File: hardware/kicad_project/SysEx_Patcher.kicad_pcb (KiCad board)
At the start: 2 copper layers, 135 x 118 mm, 83 parts, among them J1 MIDI_IN, J10 JACK6.35_pot_deporte, J2 MIDI_OUT, J3 DC_5V, J4 BAT_PWR, J5 OLED, J6 MEGA_AN, J7 MEGA_DIG, J8 MEGA_PWR, J9 MUX_SPARE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

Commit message: hardware: fully route the PCB (4 layers + GND plane)
Re-placed for routability (each RC filter beside its pot, 4067 inside the
board) and autorouted: 130/130 connections routed, DRC clean (no unconnected,
shorts, clearance or courtyard violations). 4-layer stackup with a GND plane.
Only cosmetic silkscreen-text overlaps remain.
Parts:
- removed J6: MEGA_AN, Connector_PinHeader_2.54mm:PinHeader_1x16_P2.54mm_Vertical
- removed J7: MEGA_DIG, Connector_PinHeader_2.54mm:PinHeader_1x16_P2.54mm_Vertical
- removed J9: MUX_SPARE, Connector_PinHeader_2.54mm:PinHeader_1x14_P2.54mm_Vertical
- added J6A: AN_row0, Connector_PinHeader_2.54mm:PinHeader_1x04_P2.54mm_Vertical, F.Cu at (186.0, 34.0)
- added J6B: AN_row1, Connector_PinHeader_2.54mm:PinHeader_1x04_P2.54mm_Vertical, F.Cu at (186.0, 64.0)
- added J6C: AN_row2, Connector_PinHeader_2.54mm:PinHeader_1x04_P2.54mm_Vertical, F.Cu at (186.0, 94.0)
- added J6D: AN_row3, Connector_PinHeader_2.54mm:PinHeader_1x04_P2.54mm_Vertical, F.Cu at (186.0, 124.0)
- added J7A: DIG_btnled, Connector_PinHeader_2.54mm:PinHeader_1x08_P2.54mm_Vertical, F.Cu at (34.0, 70.0)
- added J7B: DIG_midi, Connector_PinHeader_2.54mm:PinHeader_1x02_P2.54mm_Vertical, F.Cu at (130.0, 162.0)
- added J7C: DIG_i2c, Connector_PinHeader_2.54mm:PinHeader_1x02_P2.54mm_Vertical, F.Cu at (150.0, 162.0)
- added J7D: DIG_muxsel, Connector_PinHeader_2.54mm:PinHeader_1x04_P2.54mm_Vertical, F.Cu at (100.0, 150.0)
- J10: value JACK6.35_pot_deporte -> JACK6.35
- moved D2 247.0 mm to (188.0, 6.00)
- moved J4 236.3 mm to (195.0, 15.0)
- moved J5 206.5 mm to (150.0, 9.00)
- moved R2 172.2 mm to (132.0, 5.00)
- moved C1 170.8 mm to (96.0, 9.00)
- moved R3 163.2 mm to (132.0, 13.0)
- moved R25 157.3 mm to (159.0, 120.0), turned to 90 degrees
- moved C17 151.5 mm to (166.0, 120.0), turned to 90 degrees
- moved J8 147.7 mm to (160.0, 150.0)
- moved R21 139.5 mm to (159.0, 90.0), turned to 90 degrees
- moved C13 134.2 mm to (166.0, 90.0), turned to 90 degrees
- moved R20 132.4 mm to (125.0, 90.0), turned to 90 degrees
- moved R17 127.3 mm to (159.0, 60.0), turned to 90 degrees
- moved C12 127.1 mm to (132.0, 90.0), turned to 90 degrees
- moved C9 122.7 mm to (166.0, 60.0), turned to 90 degrees
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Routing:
- net +5V: track 0.00 -> 706.6 mm, vias 0 -> 1
- net VIN_RAW: track 0.00 -> 194.7 mm
- net D0_RX: track 0.00 -> 165.5 mm
- net D1_TX: track 0.00 -> 156.6 mm
- net D21_SCL: track 0.00 -> 152.3 mm
- net MUX_CH0: track 0.00 -> 150.0 mm, vias 0 -> 1
- net D20_SDA: track 0.00 -> 148.1 mm
- net A1: track 0.00 -> 142.1 mm
- net A2: track 0.00 -> 140.9 mm
- net A0: track 0.00 -> 137.7 mm
- net A3: track 0.00 -> 137.6 mm
- net A15: track 0.00 -> 123.6 mm
- net A4: track 0.00 -> 108.8 mm
- net A6: track 0.00 -> 107.8 mm
- net A5: track 0.00 -> 104.8 mm
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- added copper zone on B.Cu, net GND
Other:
- board size 135 x 118 mm -> 218 x 185 mm
- copper layers 2 -> 4

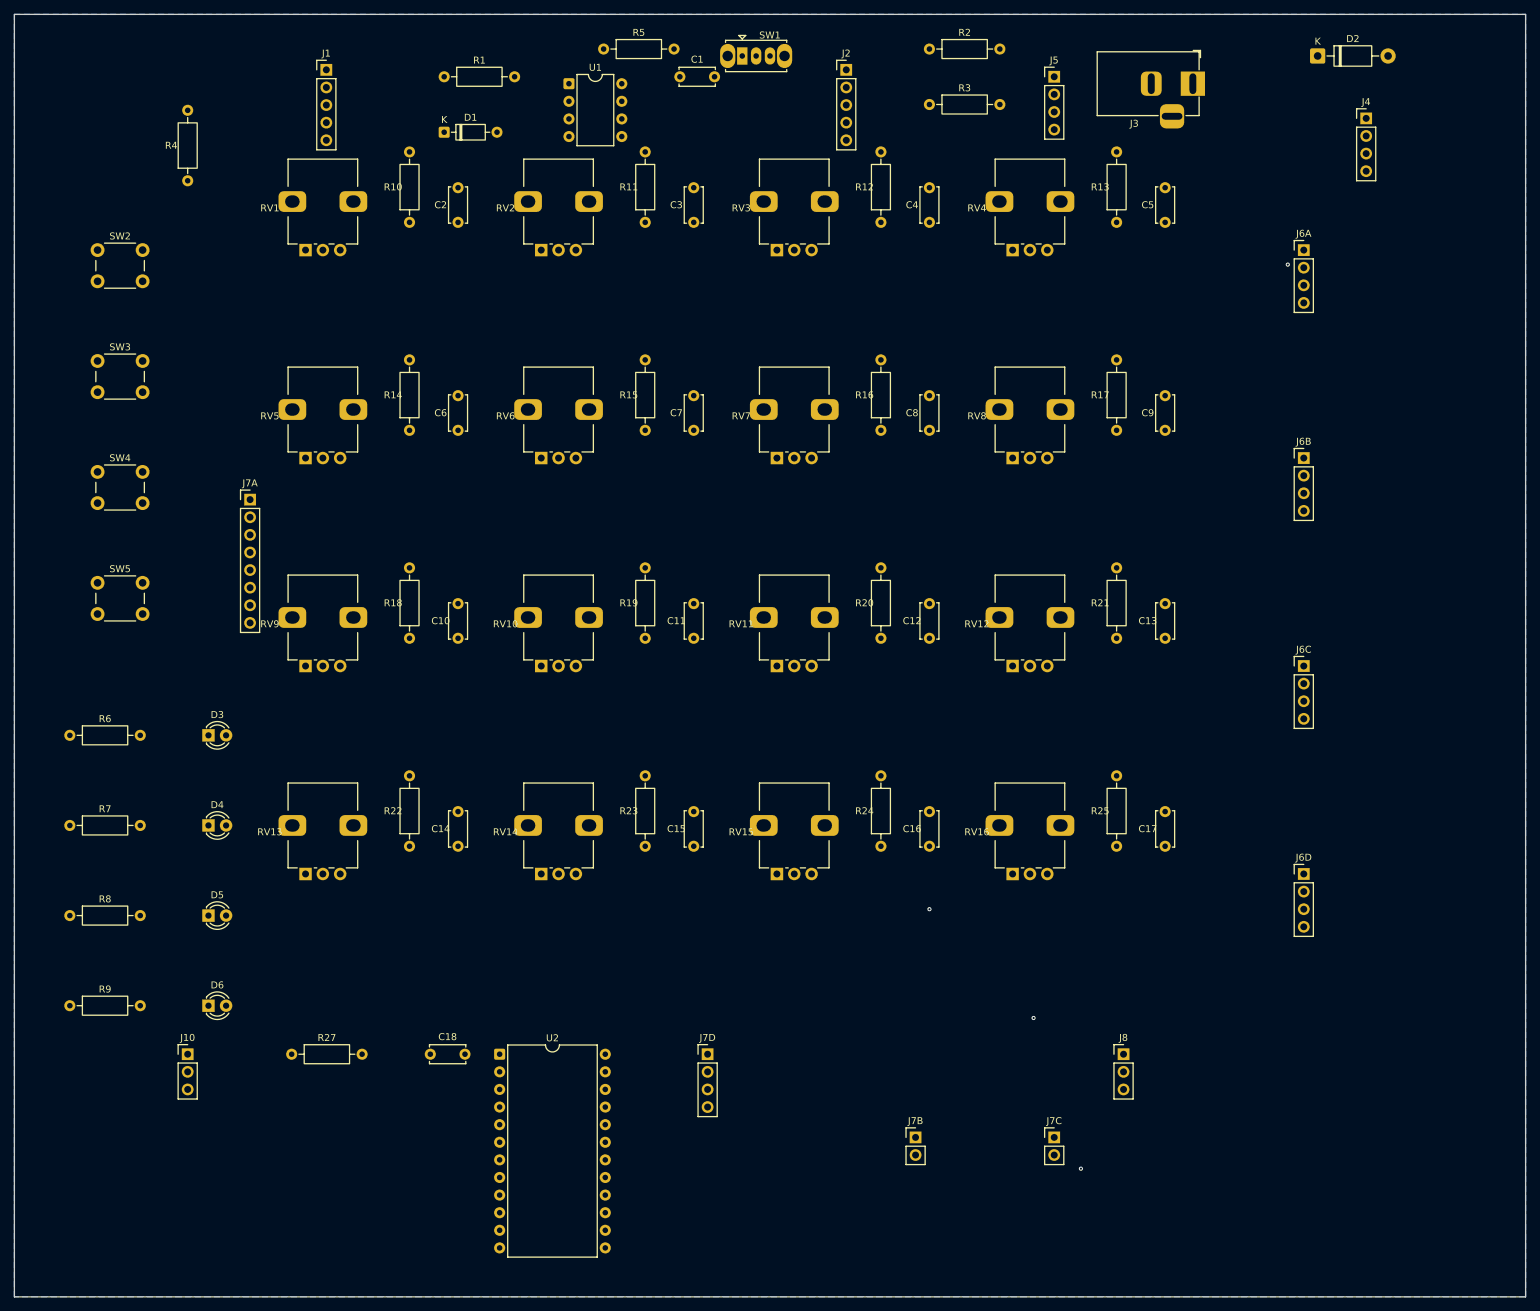
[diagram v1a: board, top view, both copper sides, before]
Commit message: hardware: compact board to 212x180mm, rounded corners, + fab Gerbers
Trimmed the board and added 5mm rounded corners (Edge.Cuts arcs). Re-routed
clean on the smaller outline (130/130 nets, DRC clean apart from cosmetic silk).
Added the fabrication package: 4-layer Gerbers + Excellon drill + job file
(hardware/fab/ and SysEx_Patcher_GERBERS.zip), ready for JLCPCB.
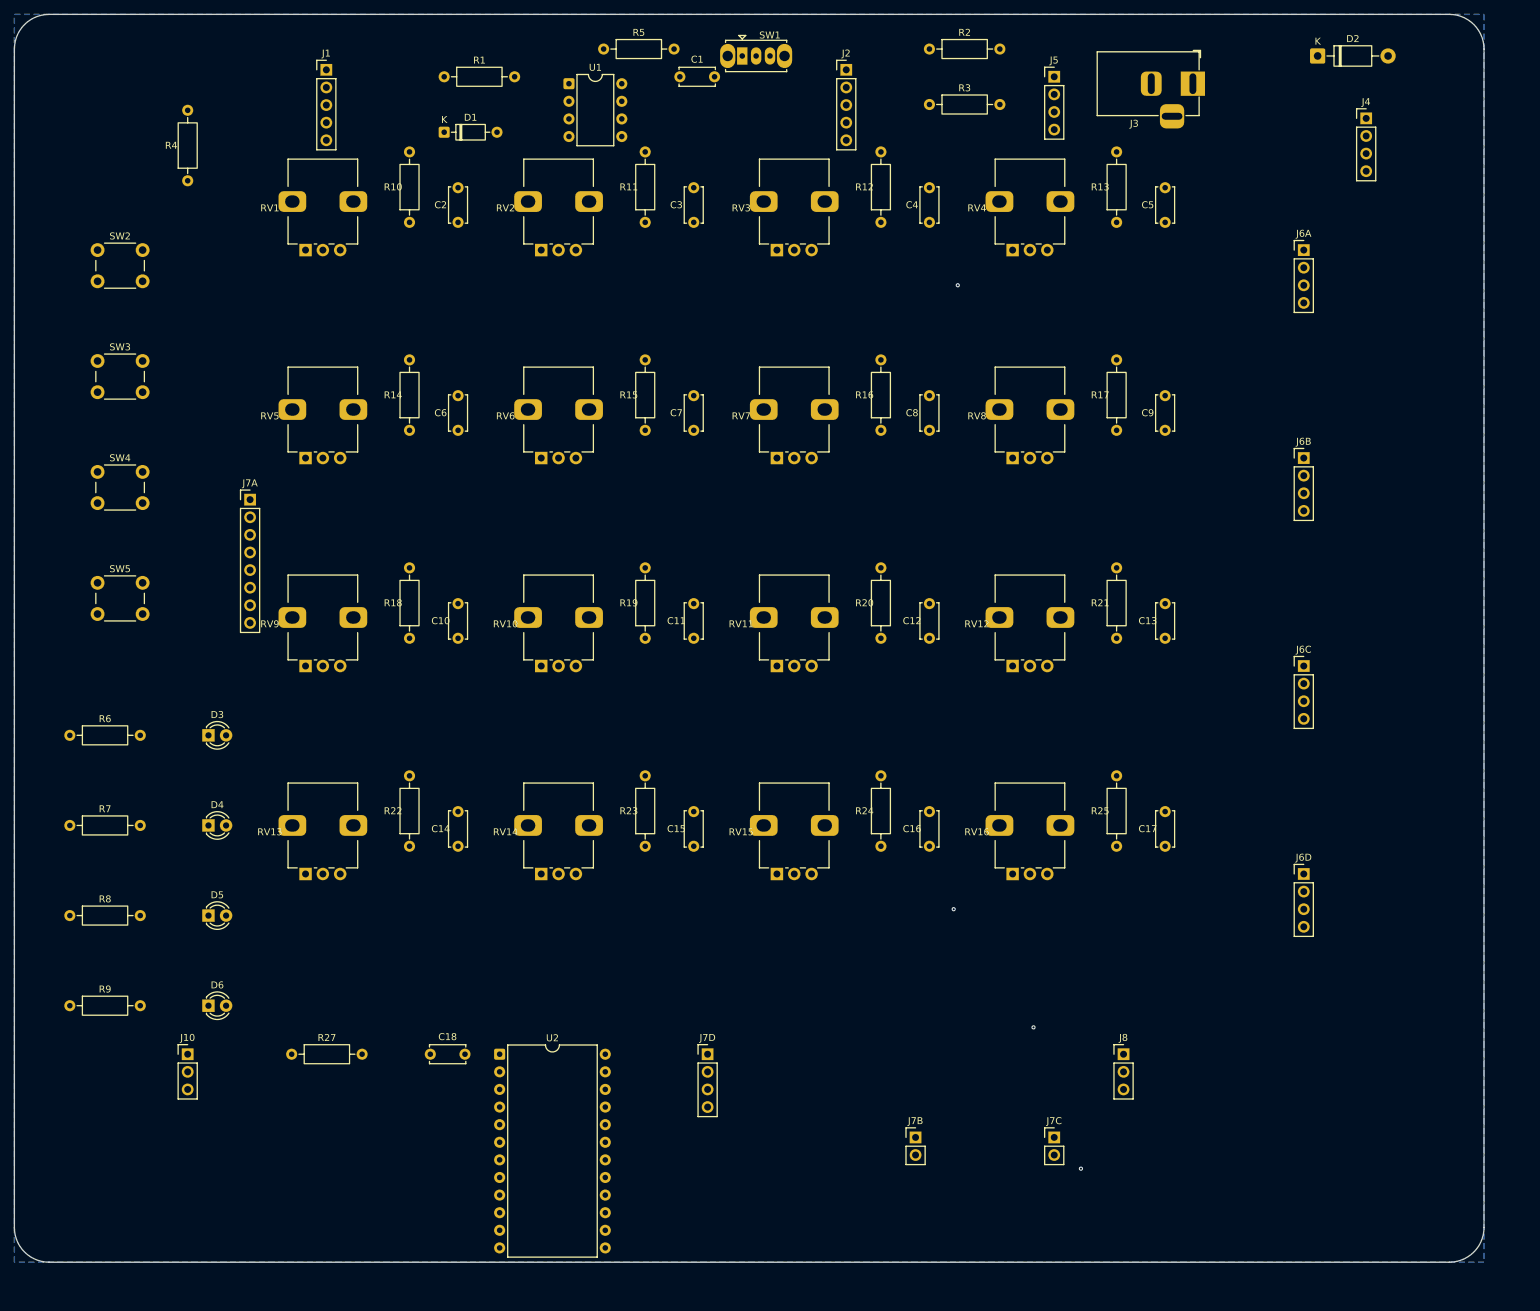
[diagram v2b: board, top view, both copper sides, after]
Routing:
- net A8: track 71.2 -> 73.7 mm
- net A11: track 76.1 -> 74.1 mm
- net A1: track 142.1 -> 140.9 mm
- net A4: track 108.8 -> 107.8 mm
- net +5V: track 706.6 -> 707.4 mm
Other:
- board size 218 x 185 mm -> 212 x 180 mm
